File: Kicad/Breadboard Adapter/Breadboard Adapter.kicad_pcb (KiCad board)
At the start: 2 copper layers, 25.4 x 105.4 mm, 6 parts, among them J1 Bus_ISA_8bit, J2 USB_C_Receptacle_USB2.0, J3 Conn_01x31, J4 Conn_01x31, J9 Bus_ISA_8bit, SW1 SW_Push_DPDT

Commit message: update adapter
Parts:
- added J5: Bus_ISA_8bit, My:8-bit-ISA, F.Cu at (116.8, 38.1)
- moved J9 45.7 mm to (137.2, 38.1)
- moved J4 41.9 mm to (148.6, 38.1)
- moved J1 12.7 mm to (96.5, 38.1)
- moved J3 8.89 mm to (90.2, 38.1)
- moved J2 1.80 mm to (97.5, 16.5)
- moved SW1 1.80 mm to (96.3, 32.2)
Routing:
- net /GND: track 164.5 -> 250.9 mm
- net /A7: track 19.9 -> 98.2 mm
- net /IRQ4: track 19.9 -> 98.2 mm
- net /5+: track 123.9 -> 180.5 mm, vias 4 -> 3
- net /A5: track 19.9 -> 49.1 mm
- net /A3: track 19.9 -> 49.1 mm
- net /A10: track 19.9 -> 49.1 mm
- net /D7: track 19.9 -> 49.1 mm
- net /D0: track 19.9 -> 49.1 mm
- net /A9: track 19.9 -> 49.1 mm
- net /A16: track 19.9 -> 49.1 mm
- net /A11: track 19.9 -> 49.1 mm
- net /A0: track 19.9 -> 49.1 mm
- net /A8: track 19.9 -> 49.1 mm
- net /A6: track 19.9 -> 49.1 mm
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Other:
- board size 25.4 x 105.4 mm -> 61.2 x 105.4 mm

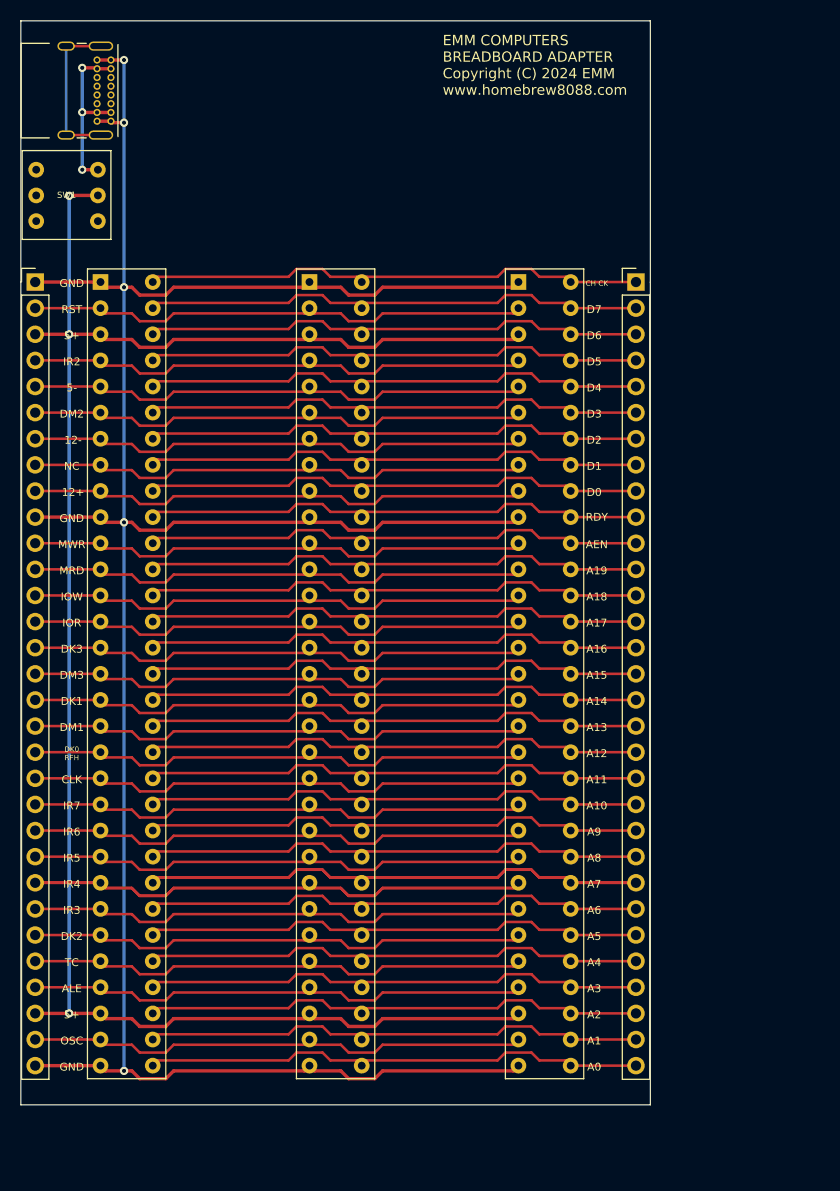
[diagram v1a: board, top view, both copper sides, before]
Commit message: Up dated Breadboard adpater
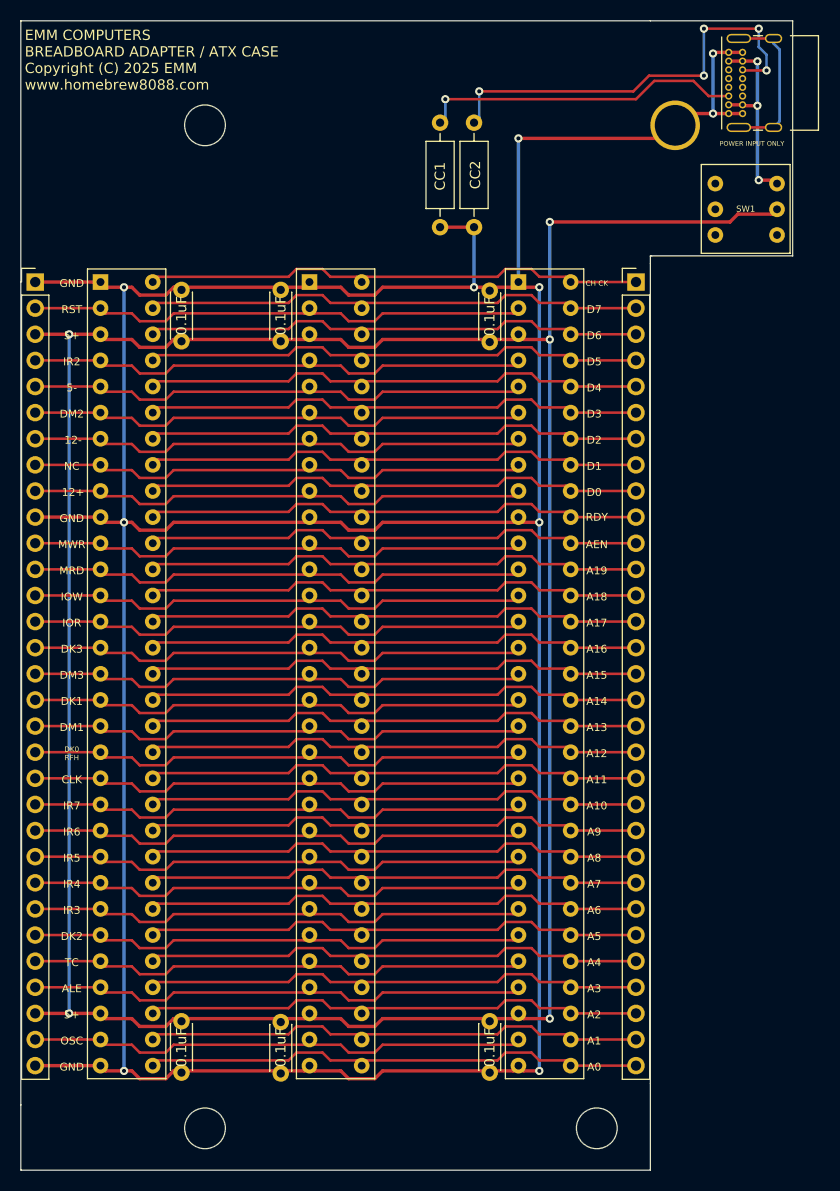
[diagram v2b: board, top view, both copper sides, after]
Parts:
- added C1: 0.1uF, Capacitor_THT:C_Disc_D4.3mm_W1.9mm_P5.00mm, F.Cu at (104.4, 38.9)
- added C2: 0.1uF, Capacitor_THT:C_Disc_D4.3mm_W1.9mm_P5.00mm, F.Cu at (104.4, 115.0)
- added C3: 0.1uF, Capacitor_THT:C_Disc_D4.3mm_W1.9mm_P5.00mm, F.Cu at (114.0, 38.9)
- added C4: 0.1uF, Capacitor_THT:C_Disc_D4.3mm_W1.9mm_P5.00mm, F.Cu at (114.0, 115.1)
- added C5: 0.1uF, Capacitor_THT:C_Disc_D4.3mm_W1.9mm_P5.00mm, F.Cu at (134.4, 38.9)
- added C6: 0.1uF, Capacitor_THT:C_Disc_D4.3mm_W1.9mm_P5.00mm, F.Cu at (134.4, 115.0)
- added R1: CC1, Resistor_THT:R_Axial_DIN0207_L6.3mm_D2.5mm_P10.16mm_Horizontal, F.Cu at (129.5, 32.8)
- added R2: CC2, Resistor_THT:R_Axial_DIN0207_L6.3mm_D2.5mm_P10.16mm_Horizontal, F.Cu at (132.8, 32.8)
- added REF**: MountingHole_3.7mm, MountingHole:MountingHole_3.7mm, F.Cu at (144.8, 120.4)
- added REF**: MountingHole_3.7mm, MountingHole:MountingHole_3.7mm, F.Cu at (106.7, 120.4)
- added REF**: MountingHole_3.7mm, MountingHole:MountingHole_3.7mm, F.Cu at (152.4, 22.9)
- added REF**: MountingHole_3.7mm, MountingHole:MountingHole_3.7mm, F.Cu at (106.7, 22.9)
- moved SW1 66.1 mm to (162.3, 33.5)
- moved J2 60.3 mm to (157.6, 21.7), turned to 90 degrees
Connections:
- J2 pad A5: Net-(J2-PadA5) -> /R1
- J2 pad B5: Net-(J2-PadB5) -> /R2
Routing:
- net /GND: track 250.9 -> 362.6 mm, vias 5 -> 10
- net /5+: track 180.5 -> 272.3 mm, vias 3 -> 5
- net /IRQ4: track 98.2 -> 49.1 mm
- net /A7: track 98.2 -> 49.1 mm
- net /R2: track 0.00 -> 42.4 mm, vias 0 -> 5
- net /R1: track 0.00 -> 31.4 mm, vias 0 -> 1
- net /POWER_SUPPLY: track 17.0 -> 19.1 mm
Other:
- board size 61.2 x 105.4 mm -> 75.1 x 111.8 mm
- board text added: "EMM COMPUTERS BREADBOARD ADAPTER / ATX CASE Copyright (C) 2025 EMM www.homebrew8088.com"
- board text added: "POWER INPUT ONLY"
- board text removed: "EMM COMPUTERS BREADBOARD ADAPTER Copyright (C) 2024 EMM www.homebrew8088.com"
